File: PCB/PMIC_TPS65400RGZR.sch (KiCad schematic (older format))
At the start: 19 parts

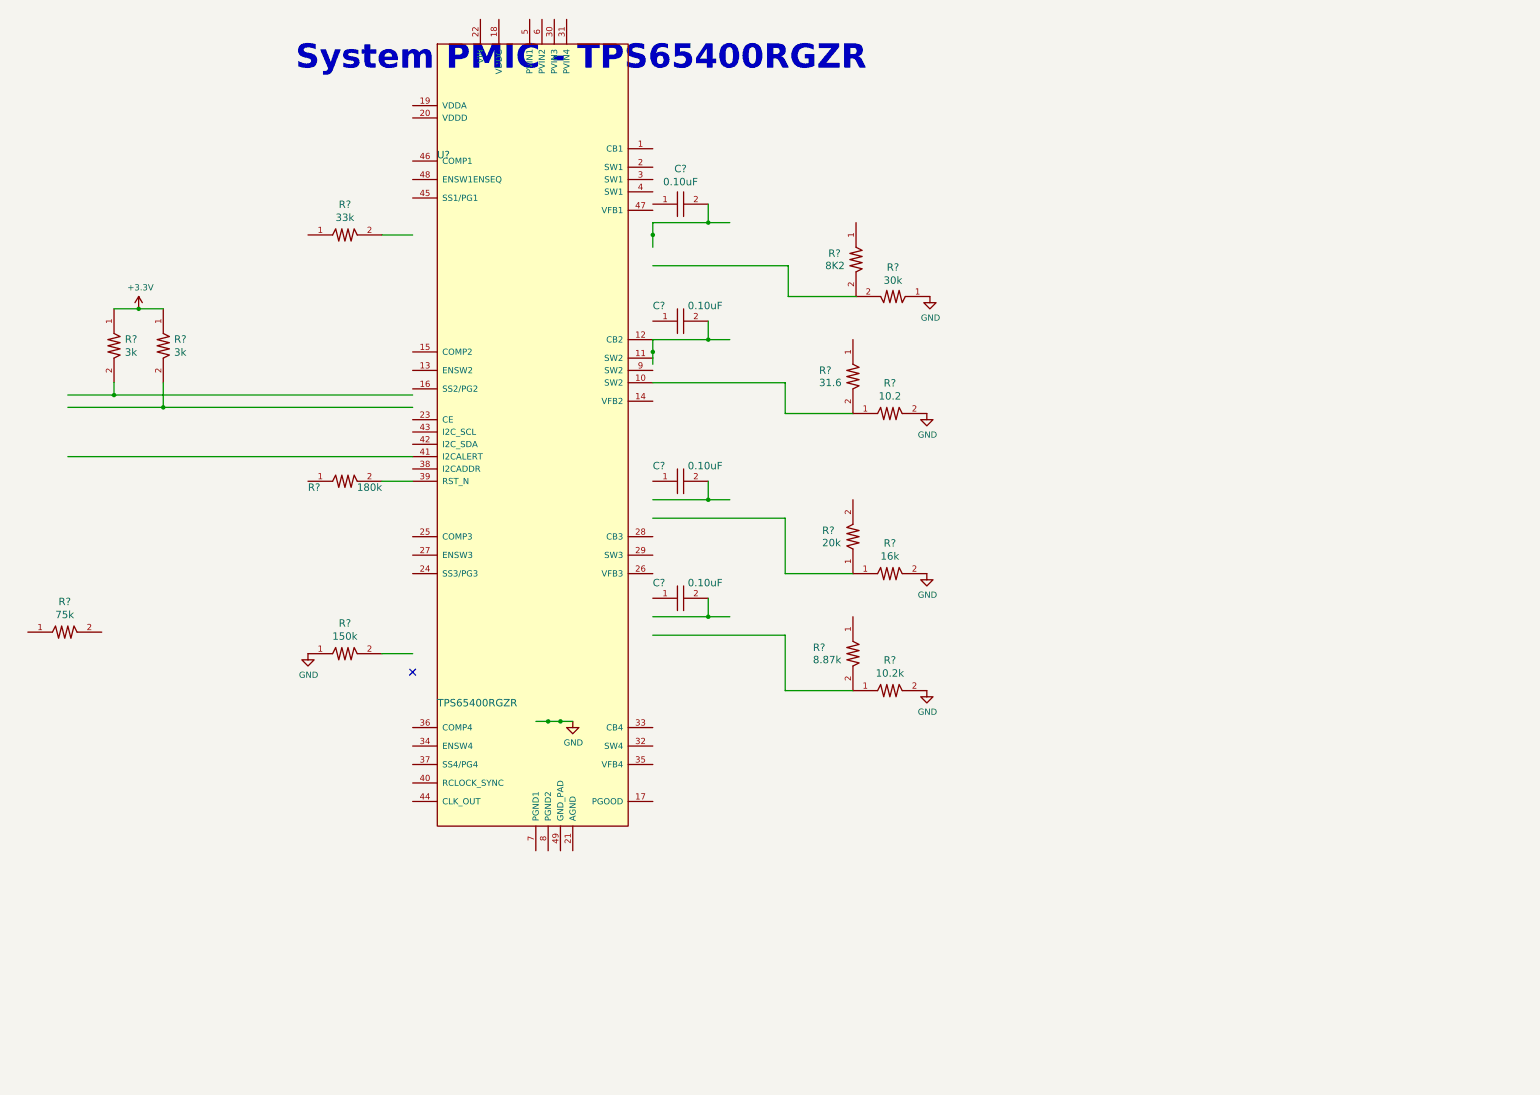
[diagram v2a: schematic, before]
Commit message: Datasheets and PMIC
PMIC schematic major progress, more datasheets for parts added to repo
for documentation purposes.
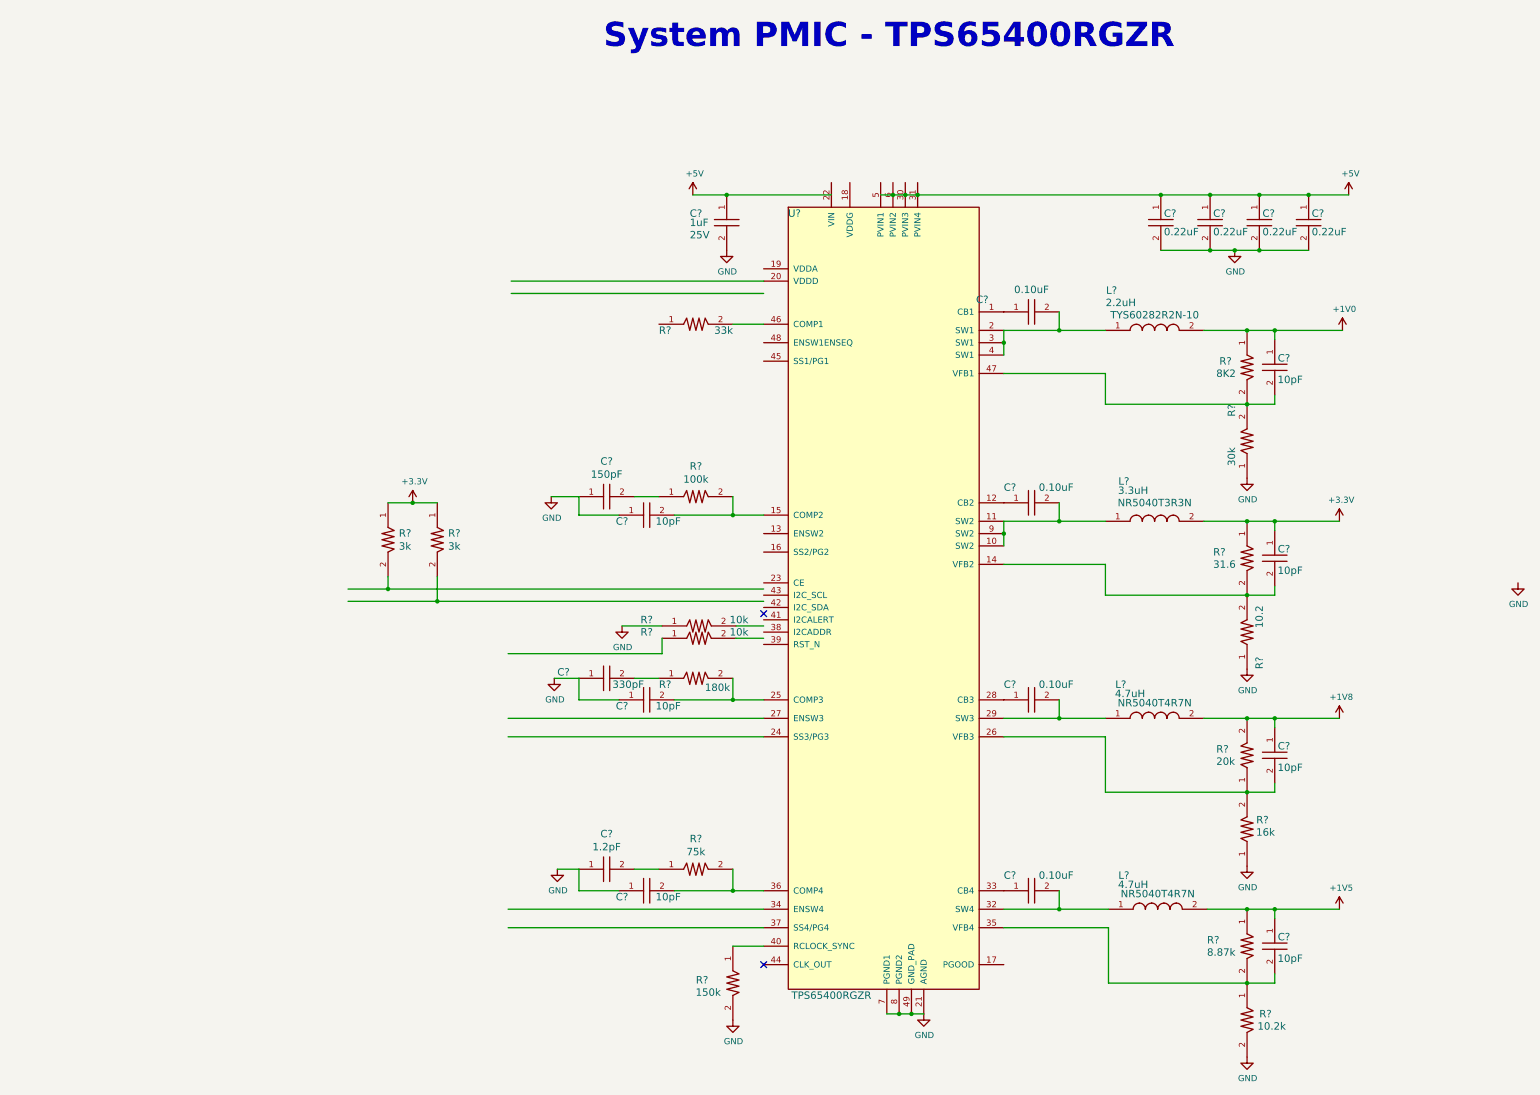
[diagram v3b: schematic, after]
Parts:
- added C?: GRM1555C1H151FA01D, PCB_Footprints:C0402, symbol GRM1555C1H151FA01D
- added C?: GRM1555C1H331FA01J, PCB_Footprints:C0402, symbol GRM1555C1H331FA01J
- added C? (x7): GQM1885C1H100RB01D, PCB_Footprints:C0603, symbol GQM1885C1H100RB01D
- added C? (x4): CL05A224KP5NNNC, PCB_Footprints:C0402, symbol CL05A224KP5NNNC
- added C?: GJM1555C1H1R2WB01D, PCB_Footprints:C0402, symbol GJM1555C1H1R2WB01D
- added C?: CL05A105KA5NQNC, PCB_Footprints:C0402, symbol CL05A105KA5NQNC
- added L?: TYS60282R2N-10, PCB_Footprints:TYS60282R2N-10, symbol TYS60282R2N-10
- added L?: NR5040T3R3N, PCB_Footprints:TYS60282R2N-10, symbol NR5040T3R3N
- added L? (x2): NR5040T4R7N, PCB_Footprints:NR5040T4R7N, symbol NR5040T4R7N
- added R?: ERJ-2RKF1003X, PCB_Footprints:R0402, symbol ERJ-2RKF1003X
- added R? (x2): RC1005F103CS, PCB_Footprints:R0402, symbol RC1005F103CS
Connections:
- net labels added: +1V0, +1V5, +1V8, +5V
- wire segments 43 -> 74
- no-connect marks 1 -> 2
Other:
- moved on the sheet: C?, R?, U?

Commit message: PMIC
PMIC component selection/creation and schematic completed.
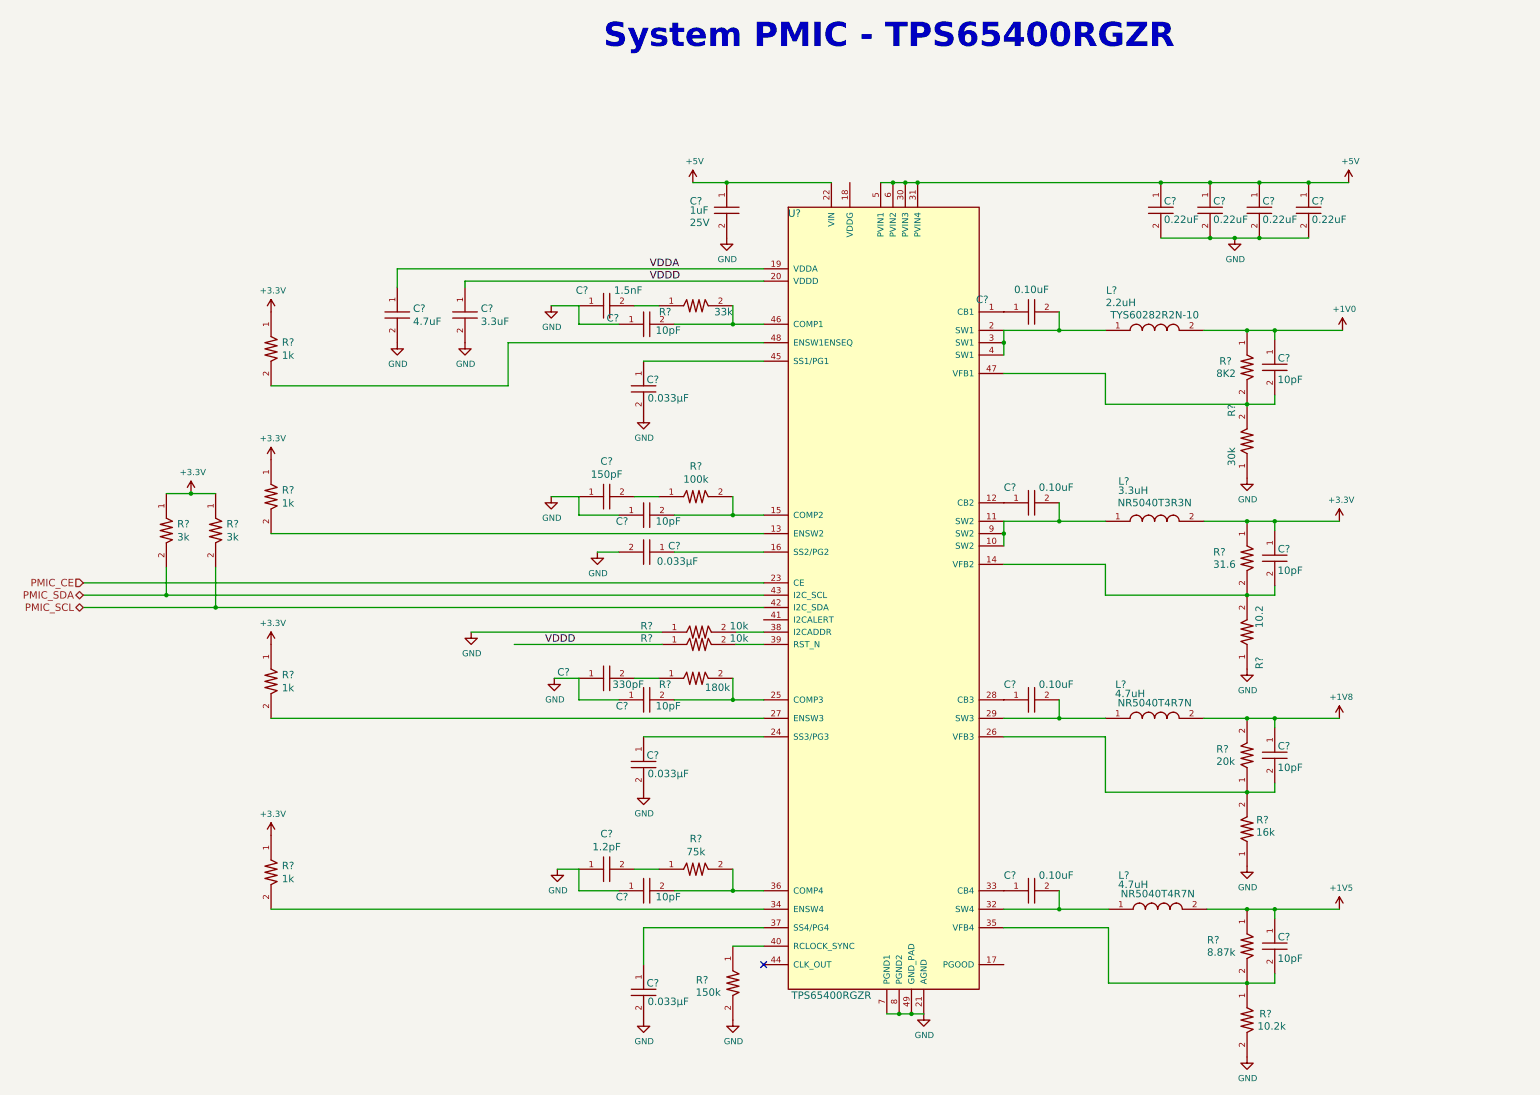
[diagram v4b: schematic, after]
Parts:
- added C?: CL05A475KQ5NRNC, PCB_Footprints:C0402, symbol CL05A475KQ5NRNC
- added C?: C0402C152J8JAC7867, PCB_Footprints:C0402, symbol C0402C152J8JAC7867
- added C?: GQM1885C1H100RB01D, PCB_Footprints:C0603, symbol GQM1885C1H100RB01D
- added C? (x4): C0402C333J4RACTU, PCB_Footprints:C0402, symbol C0402C333J4RACTU
- added C?: C1005X5R0J335K050BC, PCB_Footprints:C0402, symbol C1005X5R0J335K050BC
- added R? (x4): RC1005F102CS, PCB_Footprints:R0402, symbol RC1005F102CS
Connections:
- net labels added: PMIC_CE, PMIC_SCL, PMIC_SDA, VDDA, VDDD
- wire segments 74 -> 89
- no-connect marks 2 -> 1
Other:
- moved on the sheet: C?, R?
